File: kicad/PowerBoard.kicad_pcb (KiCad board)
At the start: 2 copper layers, 150 x 150 mm, 148 parts, among them IC1 LT1910ES8#PBF, IC2 LT1910ES8#PBF, IC3 LT1910ES8#PBF, IC4 LT1910ES8#PBF, IC5 LT1910ES8#PBF, IC7 MAX17541GATB+T, J1 XT90, J10 XT90, J11 XT90, J12 XT90, J13 XT90, J14 DEAN_T, J15 DEAN_T, J16 DEAN_T, J17 DEAN_T, J18 DEAN_T, J19 DEAN_T, J2 DEAN_T, J20 XT60, J21 XT60, J22 XT60, J23 XT60, J24 XT60, J25 XT60, J26 XT60, J27 XT60, J28 XT60, J29 XT60, J3 XT60, J30 XT60, J31 XT60, J32 XT30, J33 XT30, J34 XT30, J35 XT30, J36 XT30, J37 XT30, J38 XT30, J39 XT30, J4 XT30, J40 XT30, J41 XT60, J5 Conn_01x02, J6 XT90, J7 XT90, J8 XT90, J9 XT90, Q1 IRFS7530TRL7PP, Q2 IRFS7437TRLPBF, Q3 IRFS7437TRLPBF, Q4 IRFS7437TRLPBF, Q5 IRFS7437TRLPBF, U1 Pico, U2 INA238, U3 INA238, U4 INA238, U5 INA238, U6 INA238

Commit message: Add first firmware version
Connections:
- D20 pad 2: +42V -> 42_SHUNT
- Q1 pad 4: Net-(Q1-D) -> 42_SHUNT
- R1 pad 4: Net-(Q1-D) -> 42_SHUNT
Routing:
- net 42_SHUNT: track 0.00 -> 136.6 mm
- net +42V: track 110.2 -> 17.7 mm
- net Net-(Q1-D): track 10.3 -> 0.00 mm
- net CURR_2+: track 60.3 -> 54.8 mm
- net CURR_3+: track 66.6 -> 61.9 mm
- net CURR_4+: track 41.8 -> 37.2 mm
- net CURR_5+: track 34.7 -> 30.2 mm
- added copper zone on F.Cu, net +42V
- added copper zone on F.Cu, net 42_SHUNT
- added copper zone on F.Cu, net CURR_2+
- added copper zone on F.Cu, net CURR_3+
- added copper zone on F.Cu, net CURR_4+
- added copper zone on F.Cu, net CURR_5+

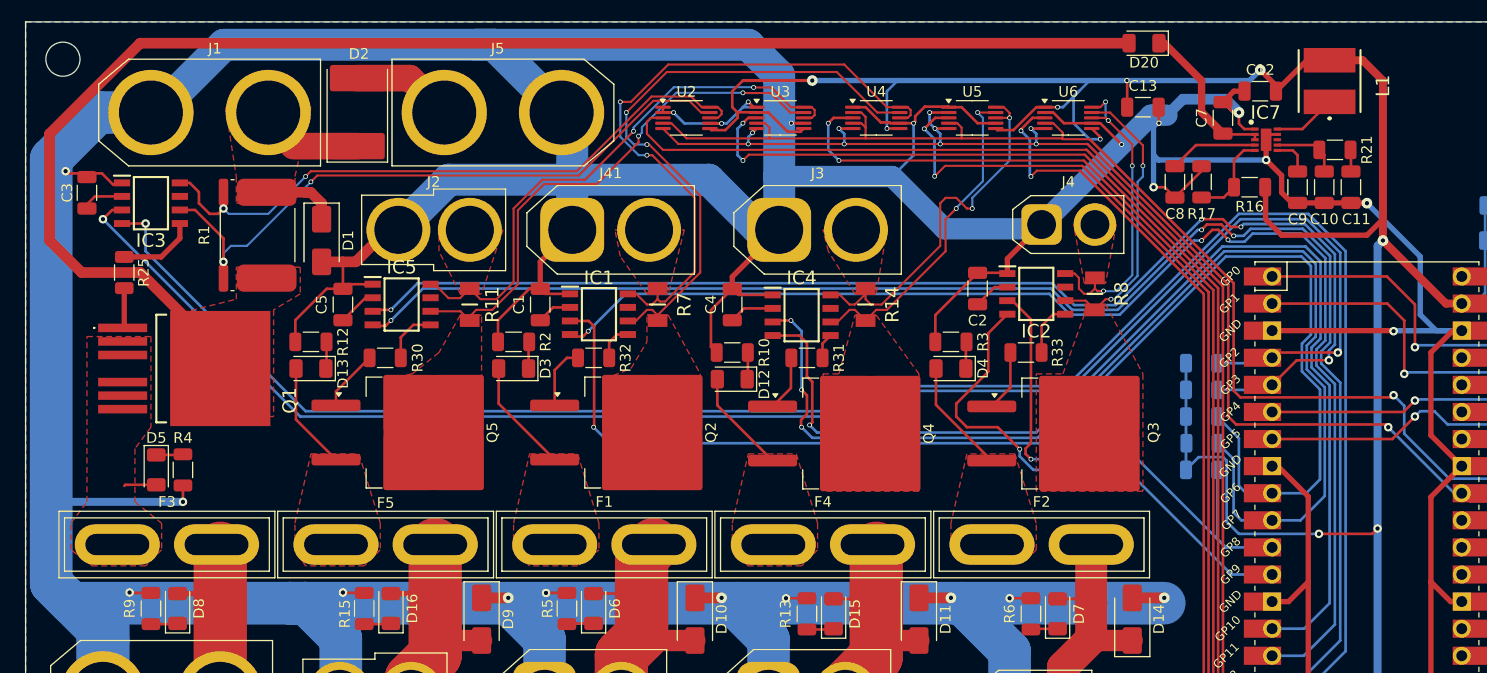
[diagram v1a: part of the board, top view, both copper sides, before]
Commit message: Add dV/dt for inrush current limitation on the main power line
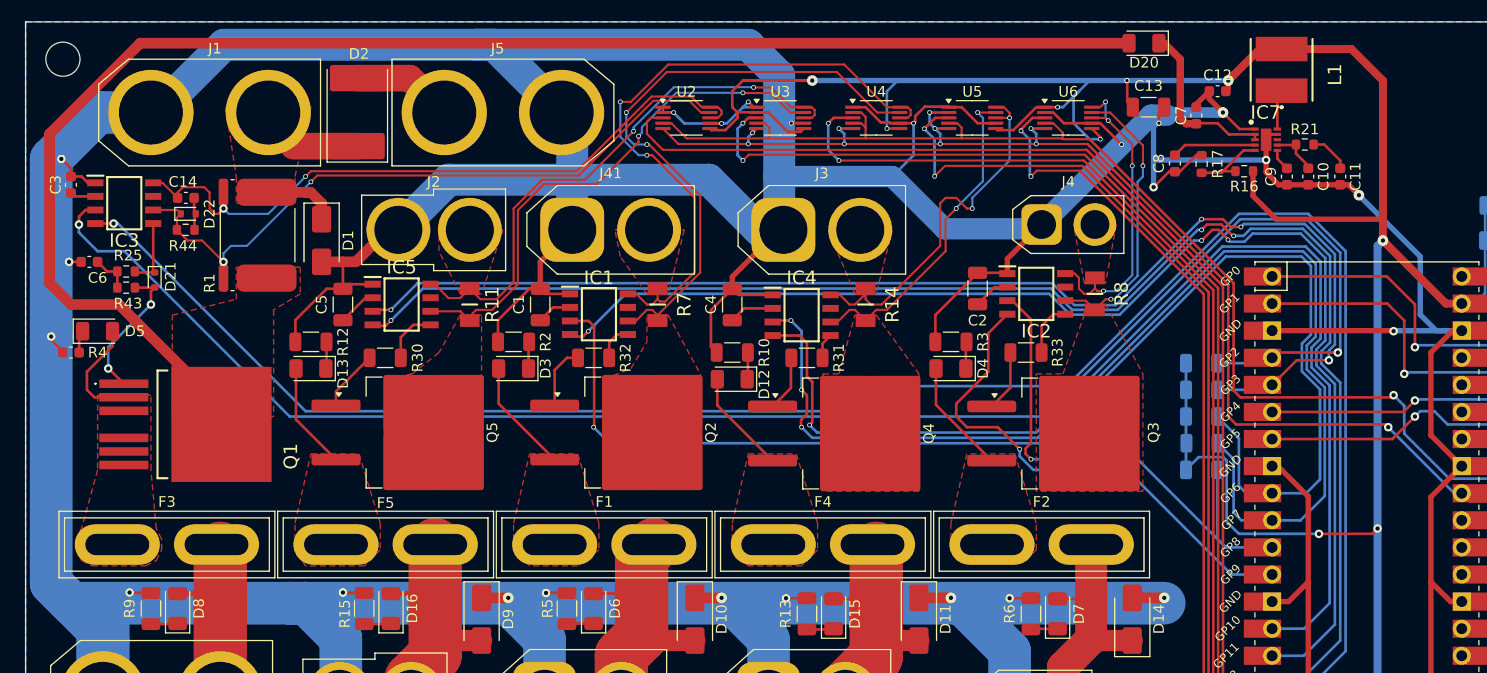
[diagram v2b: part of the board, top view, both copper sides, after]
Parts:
- added C14: 1u, Capacitor_SMD:C_0603_1608Metric, F.Cu at (40.3, 34.5)
- added C6: 1u, Capacitor_SMD:C_0603_1608Metric, F.Cu at (31.2, 40.5)
- added D21: 1N4148WT, Diode_SMD:D_SOD-523, F.Cu at (37.4, 42.2)
- added D22: 1N4148WT, Diode_SMD:D_SOD-523, F.Cu at (40.5, 36.0)
- added R43: 100k, Resistor_SMD:R_0603_1608Metric, F.Cu at (34.7, 42.9)
- added R44: 10k, Resistor_SMD:R_0603_1608Metric, F.Cu at (40.3, 37.5)
- C1, C2, C4, C5: value 1u -> 0.1u
- C10, C11, C12, C3, C7, C8, C9: footprint Capacitor_SMD:C_1206_3216Metric -> Capacitor_SMD:C_0603_1608Metric
- R16, R17, R21: footprint Resistor_SMD:R_1206_3216Metric -> Resistor_SMD:R_0603_1608Metric
- R25: value 100 -> 100k; footprint Resistor_SMD:R_1206_3216Metric -> Resistor_SMD:R_0603_1608Metric
- R4: footprint Resistor_SMD:R_1206_3216Metric -> Capacitor_SMD:C_0603_1608Metric
- moved R4 15.2 mm to (29.5, 49.0), turned to 180 degrees
- moved D5 14.1 mm to (32.0, 47.0), turned to 0 degrees
- moved Q1 5.24 mm to (40.5, 55.7)
- moved L1 4.62 mm to (143.0, 22.5)
- moved C12 4.00 mm to (137.0, 24.5)
- moved R21 2.87 mm to (145.2, 29.5)
- moved C7 2.51 mm to (135.0, 26.8)
- moved IC3 2.50 mm to (34.5, 35.0)
- moved C10 1.80 mm to (145.5, 32.5)
- moved C8 1.73 mm to (133.0, 31.3)
- moved C3 1.68 mm to (29.5, 33.3)
- moved R17 1.68 mm to (135.5, 31.3)
- moved R16 1.58 mm to (139.5, 32.0)
- moved C11 1.41 mm to (148.5, 32.5)
- moved C9 1.41 mm to (143.5, 32.5)
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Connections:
- R25 pad 1: Net-(IC3-GATE) -> Net-(C6-Pad2)
- R25 pad 2: Net-(Q1-G) -> Net-(IC3-GATE)
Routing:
- net GND: track 1132.4 -> 1118.3 mm, vias 24 -> 25
- net Net-(Q1-G): track 3.79 -> 14.8 mm, vias 0 -> 2
- net Net-(D5-A): track 3.04 -> 10.2 mm
- net 42_SHUNT: track 136.6 -> 141.3 mm
- net CURR_1+: track 61.2 -> 65.1 mm
- net Net-(C6-Pad2): track 0.00 -> 3.74 mm
- net Net-(D22-A): track 0.00 -> 3.11 mm
- net FAULT_42V: track 156.0 -> 158.8 mm
- net CURR_1-: track 61.7 -> 64.3 mm
- net Net-(IC7-LX): track 5.96 -> 3.77 mm
- net Net-(IC7-COMP): track 6.34 -> 4.47 mm
- net Net-(C11-Pad1): track 2.04 -> 3.85 mm
- net Net-(IC7-SS): track 3.61 -> 2.05 mm
- net Net-(D20-K): track 14.8 -> 16.3 mm
- net CURR_4+: track 37.2 -> 35.9 mm
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
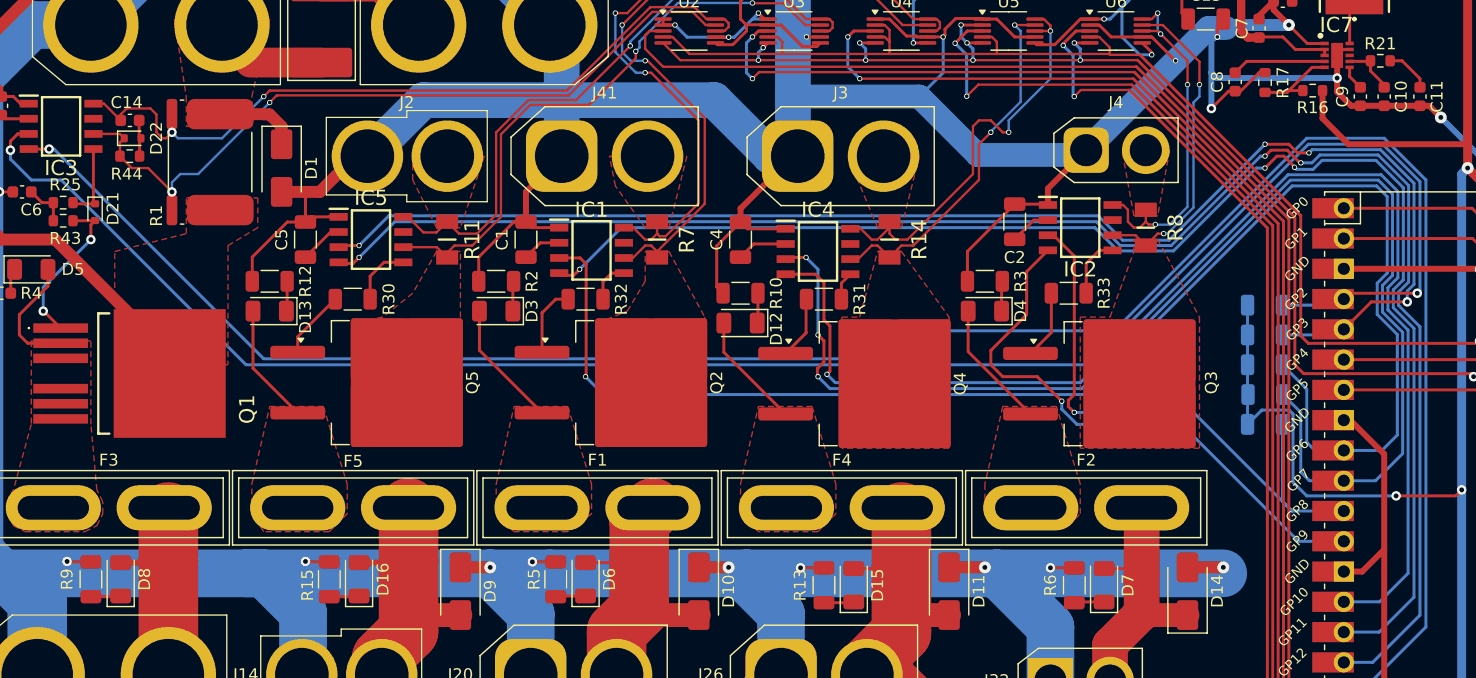
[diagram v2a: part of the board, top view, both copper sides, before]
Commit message: finish inrush current limiting
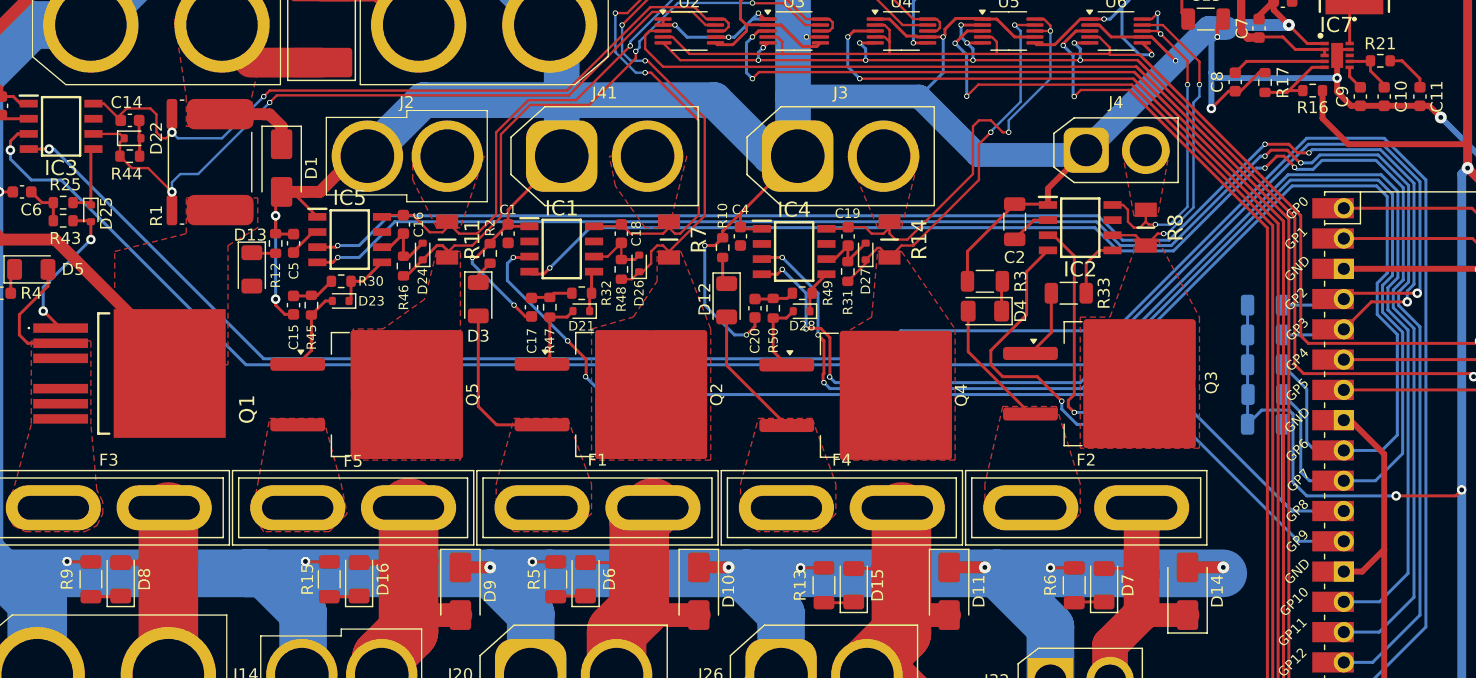
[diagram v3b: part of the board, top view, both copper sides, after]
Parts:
- added C15: 1u, Capacitor_SMD:C_0603_1608Metric, F.Cu at (54.0, 50.0)
- added C16: 1u, Capacitor_SMD:C_0603_1608Metric, F.Cu at (63.2, 43.2)
- added C17: 1u, Capacitor_SMD:C_0603_1608Metric, F.Cu at (74.0, 50.2)
- added C18: 1u, Capacitor_SMD:C_0603_1608Metric, F.Cu at (81.5, 44.0)
- added C19: 1u, Capacitor_SMD:C_0603_1608Metric, F.Cu at (100.5, 44.2)
- added C20: 1u, Capacitor_SMD:C_0603_1608Metric, F.Cu at (92.7, 50.3)
- added D23: 1N4148WT, Diode_SMD:D_SOD-523, F.Cu at (58.0, 49.6)
- added D24: 1N4148WT, Diode_SMD:D_SOD-523, F.Cu at (64.8, 45.5)
- added D25: 1N4148WT, Diode_SMD:D_SOD-523, F.Cu at (37.0, 42.3)
- added D26: 1N4148WT, Diode_SMD:D_SOD-523, F.Cu at (83.0, 46.5)
- added D27: 1N4148WT, Diode_SMD:D_SOD-523, F.Cu at (102.0, 45.5)
- added D28: 1N4148WT, Diode_SMD:D_SOD-523, F.Cu at (96.6, 50.5)
- added R45: 100k, Resistor_SMD:R_0603_1608Metric, F.Cu at (55.5, 50.0)
- added R46: 10k, Resistor_SMD:R_0603_1608Metric, F.Cu at (63.2, 46.7)
- added R47: 100k, Resistor_SMD:R_0603_1608Metric, F.Cu at (75.5, 50.2)
- added R48: 10k, Resistor_SMD:R_0603_1608Metric, F.Cu at (81.5, 47.0)
- added R49: 100k, Resistor_SMD:R_0603_1608Metric, F.Cu at (96.7, 49.0)
- added R50: 100k, Resistor_SMD:R_0603_1608Metric, F.Cu at (94.2, 50.3)
- C1, C4, C5: value 0.1u -> 1u; footprint Capacitor_SMD:C_1206_3216Metric -> Capacitor_SMD:C_0603_1608Metric
- R10, R12, R2: footprint Resistor_SMD:R_1206_3216Metric -> Resistor_SMD:R_0603_1608Metric
- R30, R32: value 100 -> 100k; footprint Resistor_SMD:R_1206_3216Metric -> Resistor_SMD:R_0603_1608Metric
- R31: value 100 -> 10k; footprint Resistor_SMD:R_1206_3216Metric -> Resistor_SMD:R_0603_1608Metric
- moved D21 41.6 mm to (78.1, 50.5), turned to 180 degrees
- moved R10 4.11 mm to (90.0, 45.2), turned to 90 degrees
- moved D13 3.81 mm to (50.5, 47.0), turned to -90 degrees
- moved R12 3.21 mm to (52.5, 44.8), turned to 90 degrees
- moved R31 3.07 mm to (100.5, 47.2), turned to -90 degrees
- moved IC1 2.50 mm to (76.5, 45.3)
- moved R2 2.39 mm to (70.5, 45.7), turned to 90 degrees
- moved D12 2.24 mm to (90.3, 49.6), turned to -90 degrees
- moved IC4 2.00 mm to (96.0, 45.5)
- moved D3 1.80 mm to (69.5, 49.5), turned to -90 degrees
- moved IC5 1.79 mm to (58.7, 44.5)
- moved R30 1.78 mm to (58.0, 48.0), turned to 0 degrees
- moved C1 1.58 mm to (72.0, 44.0)
- moved C5 1.05 mm to (54.0, 44.8)
- moved Q2 1.00 mm to (82.5, 57.5)
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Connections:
- D21 pad 1: Net-(IC3-GATE) -> /IC1-G
- D21 pad 2: Net-(Q1-G) -> /Q2-G
- IC1 pad 5: Net-(IC1-GATE) -> /IC1-G
- IC1 pad 6: CURR_3- -> /IC1-SENSE
- IC3 pad 5: Net-(IC3-GATE) -> /IC3-G
- IC4 pad 5: Net-(IC4-GATE) -> /IC4-G
- IC4 pad 6: CURR_4- -> /IC4-SENSE
- IC5 pad 5: Net-(IC5-GATE) -> /IC5-G
- IC5 pad 6: CURR_2- -> Net-(D24-A)
- Q1 pad 1: Net-(Q1-G) -> /Q1-G
- Q2 pad 1: Net-(Q2-G) -> /Q2-G
- Q2 pad 2: CURR_3- -> unconnected-(Q2-D-Pad2)
- Q4 pad 1: Net-(Q4-G) -> /Q4-G
- Q4 pad 2: CURR_4- -> unconnected-(Q4-D-Pad2)
- Q5 pad 1: Net-(Q5-G) -> /Q5-G
- R25 pad 2: Net-(IC3-GATE) -> /IC3-G
- R30 pad 1: Net-(IC5-GATE) -> Net-(C15-Pad2)
- R30 pad 2: Net-(Q5-G) -> /IC5-G
- R31 pad 1: Net-(IC4-GATE) -> /IC4-SENSE
- R31 pad 2: Net-(Q4-G) -> CURR_4-
- R32 pad 1: Net-(IC1-GATE) -> Net-(C17-Pad2)
- R32 pad 2: Net-(Q2-G) -> /IC1-G
- R43 pad 2: Net-(Q1-G) -> /Q1-G
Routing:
- net GND: track 1118.3 -> 1135.5 mm, vias 25 -> 31
- net Net-(Q1-G): track 14.8 -> 0.00 mm, vias 2 -> 0
- net /Q1-G: track 0.00 -> 14.3 mm, vias 0 -> 2
- net Net-(D13-A): track 12.6 -> 2.51 mm
- net /Q5-G: track 0.00 -> 6.85 mm
- net Net-(IC3-GATE): track 6.54 -> 0.00 mm
- net /Q2-G: track 0.00 -> 6.38 mm
- net /IC3-G: track 0.00 -> 6.37 mm
- net /Q4-G: track 0.00 -> 6.32 mm
- net Net-(D24-A): track 0.00 -> 6.22 mm
- net Net-(Q2-G): track 5.97 -> 0.00 mm
- net /IC1-SENSE: track 0.00 -> 5.82 mm
- net /IC4-SENSE: track 0.00 -> 5.81 mm
- net Net-(Q5-G): track 5.76 -> 0.00 mm
- net Net-(Q4-G): track 5.28 -> 0.00 mm
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- added copper zone on B.Cu, net GND
- added copper zone on F.Cu, net GND
- removed copper zone on B.Cu, net (none)
- removed copper zone on F.Cu, net (none)

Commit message: finish v2.4.0
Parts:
- added C21: 1u, Capacitor_SMD:C_0603_1608Metric, F.Cu at (121.0, 42.2)
- added C22: 1u, Capacitor_SMD:C_0603_1608Metric, F.Cu at (113.5, 48.2)
- added D29: 1N4148WT, Diode_SMD:D_SOD-523, F.Cu at (122.8, 44.3)
- added D30: 1N4148WT, Diode_SMD:D_SOD-523, F.Cu at (117.3, 49.0)
- added J42: DEAN_T, SamacSys_Parts:DEANS-T, F.Cu at (58.0, 144.0)
- added J43: DEAN_T, SamacSys_Parts:DEANS-T, F.Cu at (58.0, 154.5)
- added J44: XT60, Connector_AMASS:AMASS_XT60-F_1x02_P7.20mm_Vertical, F.Cu at (73.9, 144.0)
- added J45: XT60, Connector_AMASS:AMASS_XT60-F_1x02_P7.20mm_Vertical, F.Cu at (73.9, 154.5)
- added J46: XT60, Connector_AMASS:AMASS_XT60-F_1x02_P7.20mm_Vertical, F.Cu at (94.9, 155.0)
- added J47: XT30, Connector_AMASS:AMASS_XT30U-F_1x02_P5.0mm_Vertical, F.Cu at (117.5, 144.5)
- added J48: XT30, Connector_AMASS:AMASS_XT30U-F_1x02_P5.0mm_Vertical, F.Cu at (117.5, 151.5)
- added R51: 10k, Resistor_SMD:R_0603_1608Metric, F.Cu at (121.0, 45.3)
- added R52: 100k, Resistor_SMD:R_0603_1608Metric, F.Cu at (115.0, 48.2)
- C2: value 0.1u -> 1u; footprint Capacitor_SMD:C_1206_3216Metric -> Capacitor_SMD:C_0603_1608Metric
- R3: footprint Resistor_SMD:R_1206_3216Metric -> Resistor_SMD:R_0603_1608Metric
- R33: value 100 -> 100k; footprint Resistor_SMD:R_1206_3216Metric -> Resistor_SMD:R_0603_1608Metric
- moved IC2 4.00 mm to (116.0, 43.5)
- moved R3 3.75 mm to (110.0, 44.8), turned to 90 degrees
- moved C2 3.10 mm to (111.5, 42.2)
- moved R33 2.28 mm to (117.3, 47.5), turned to 0 degrees
- moved D4 2.05 mm to (110.6, 49.0), turned to -90 degrees
- moved C19 0.23 mm to (100.5, 44.0)
- turned C14 to 0 degrees
- turned D22 to 180 degrees
- turned R44 to 180 degrees
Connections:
- net Net-(D24-A) renamed /IC5-SENSE
- C14 pad 1: Net-(D22-A) -> /IC3-SENSE
- D22 pad 2: Net-(D22-A) -> /IC3-SENSE
- IC2 pad 5: Net-(IC2-GATE) -> /IC2-G
- IC2 pad 6: CURR_5- -> /IC2-SENSE
- IC3 pad 6: CURR_1- -> /IC3-SENSE
- Q2 pad 2: unconnected-(Q2-D-Pad2) -> CURR_3-
- Q3 pad 1: Net-(Q3-G) -> /Q3-G
- Q4 pad 2: unconnected-(Q4-D-Pad2) -> CURR_4-
- R33 pad 1: Net-(IC2-GATE) -> Net-(C22-Pad2)
- R33 pad 2: Net-(Q3-G) -> /IC2-G
- R44 pad 2: Net-(D22-A) -> /IC3-SENSE
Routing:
- net GND: track 1135.5 -> 1203.5 mm, vias 31 -> 33
- net 24V_2: track 76.6 -> 97.6 mm
- net 15V_2: track 77.0 -> 98.0 mm
- net 5V_2: track 78.8 -> 92.8 mm
- net 12V_2: track 95.3 -> 105.8 mm
- net /Q3-G: track 0.00 -> 6.94 mm
- net /IC2-SENSE: track 0.00 -> 6.50 mm
- net /IC3-SENSE: track 0.00 -> 6.03 mm
- net Net-(Q3-G): track 5.78 -> 0.00 mm
- net Net-(IC2-GATE): track 5.17 -> 0.00 mm
- net CURR_1-: track 64.3 -> 60.2 mm
- net /IC2-G: track 0.00 -> 3.89 mm
- net CURR_5+: track 30.2 -> 34.0 mm
- net Net-(IC2-TIMER): track 3.45 -> 0.00 mm
- net Net-(D22-A): track 3.11 -> 0.00 mm
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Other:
- board text added: "Power Board v2.4.0"
- board text removed: "Power Board v2.3.0"
